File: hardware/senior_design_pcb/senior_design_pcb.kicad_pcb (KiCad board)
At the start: 4 copper layers, 290 x 202.5 mm, 60 parts, among them J1 SBH11-PBPC-D05-ST-BK, J10 1x06Screw-Stepper Driver2, J11 2x08Rectangle-LED Matrix Conn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, J12 1x05JST - Joystick2 connector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, J13 UJ20-C-H-C-4-SMT-TR, J3 1x02JST-IR Transmitter1, J4 1x03JST- IR Receiver1, J5 1x05JST-Admin LCD Console Con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, J6 1x05JST - Joystick1 connector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, J7 1x02JST-IR Transmitter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

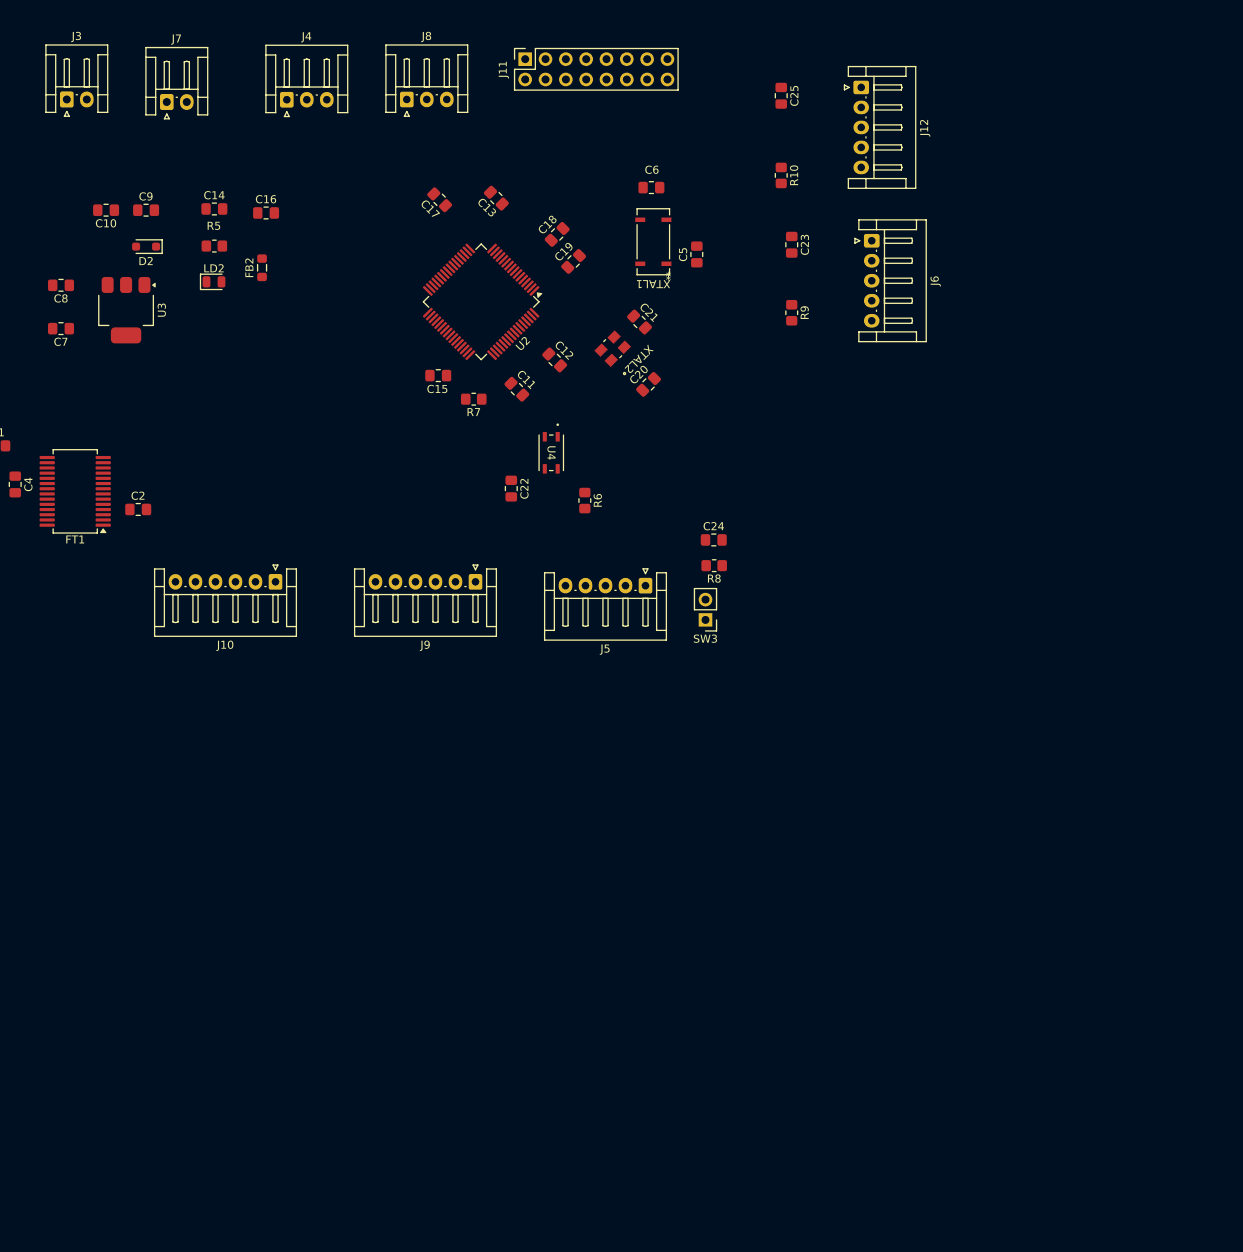
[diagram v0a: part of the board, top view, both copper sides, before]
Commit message: edited schematic pinouts
added test points
edited pinouts for easier traces
added header
added comments
+notes from class today & what to change
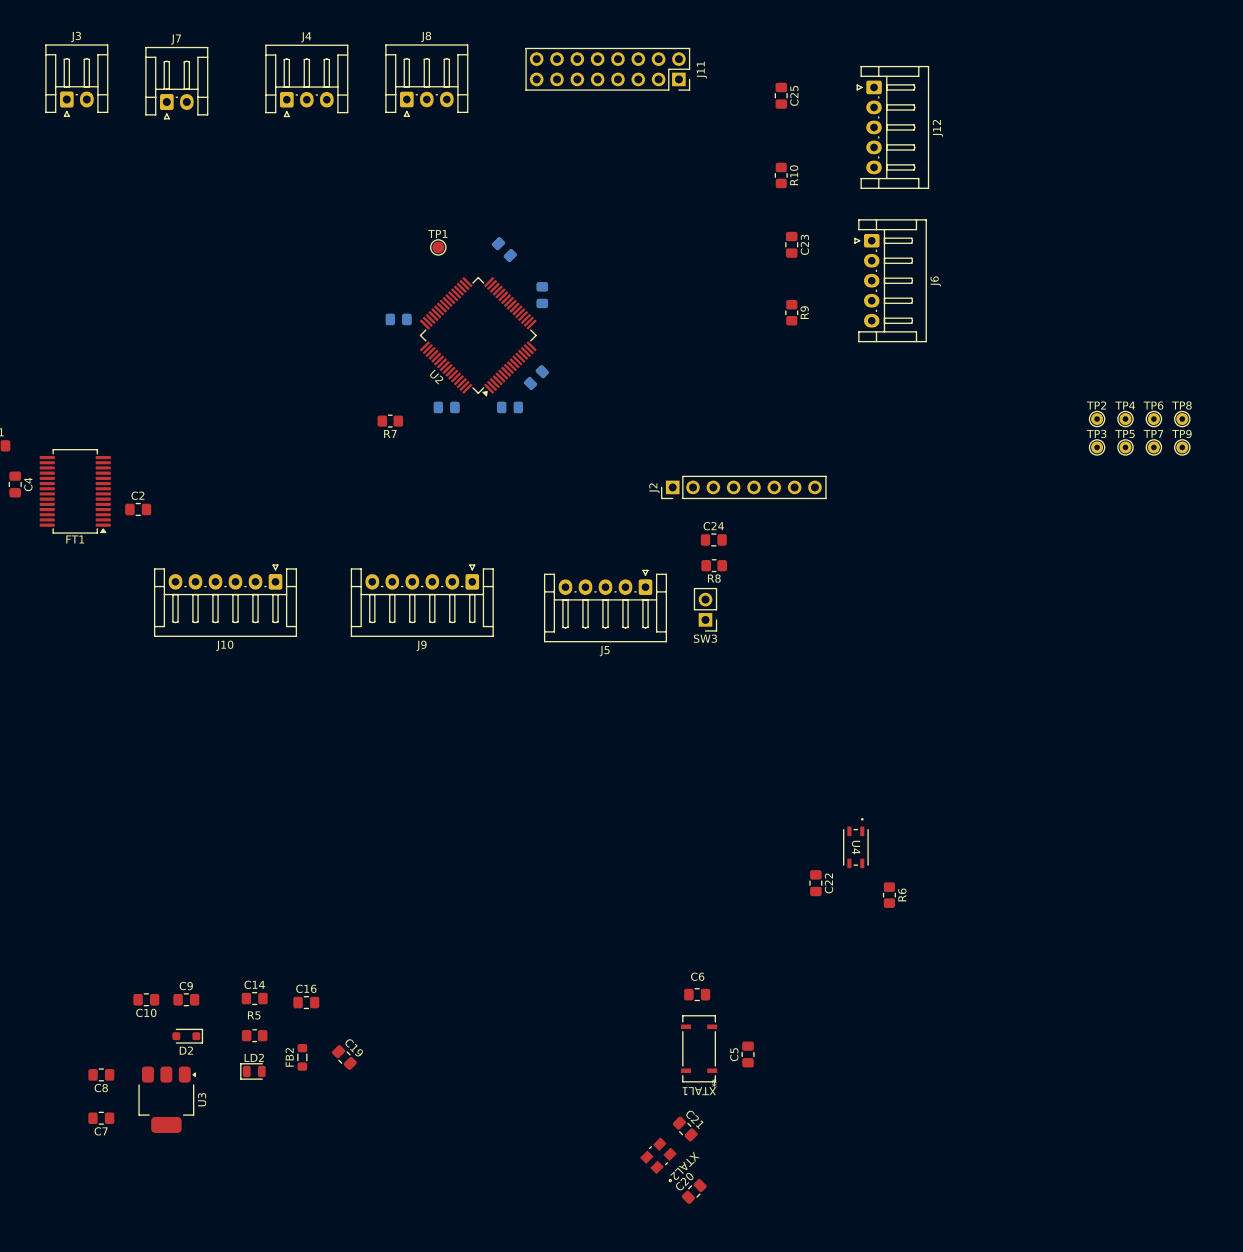
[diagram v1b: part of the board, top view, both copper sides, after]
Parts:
- added J2: Conn_01x08_Pin, Connector_PinHeader_2.54mm:PinHeader_1x08_P2.54mm_Vertical, F.Cu at (132.3, 88.0)
- added TP1: TestPoint_Small, TestPoint:TestPoint_Pad_D1.5mm, F.Cu at (103.0, 58.0)
- added TP2: TestPoint, TestPoint:TestPoint_THTPad_D1.5mm_Drill0.7mm, F.Cu at (185.3, 79.5)
- added TP3: NRST, TestPoint:TestPoint_THTPad_D1.5mm_Drill0.7mm, F.Cu at (185.3, 83.0)
- added TP4: IR-IN1, TestPoint:TestPoint_THTPad_D1.5mm_Drill0.7mm, F.Cu at (188.9, 79.5)
- added TP5: IR-IN2, TestPoint:TestPoint_THTPad_D1.5mm_Drill0.7mm, F.Cu at (188.9, 83.0)
- added TP6: VBUS, TestPoint:TestPoint_THTPad_D1.5mm_Drill0.7mm, F.Cu at (192.4, 79.5)
- added TP7: +5V, TestPoint:TestPoint_THTPad_D1.5mm_Drill0.7mm, F.Cu at (192.4, 83.0)
- added TP8: 3V3, TestPoint:TestPoint_THTPad_D1.5mm_Drill0.7mm, F.Cu at (196.0, 79.5)
- added TP9: GND, TestPoint:TestPoint_THTPad_D1.5mm_Drill0.7mm, F.Cu at (196.0, 83.0)
- C11, C12, C13, C15, C17, C18: moved to B.Cu
- moved C19 103.6 mm to (91.3, 159.3), turned to -45 degrees
- moved C21 101.0 mm to (133.9, 168.2)
- moved C6 101.0 mm to (135.4, 151.4)
- moved XTAL1 101.0 mm to (135.6, 158.2)
- moved C20 101.0 mm to (135.0, 176.0)
- moved XTAL2 101.0 mm to (130.5, 171.5)
- moved C5 100.2 mm to (141.7, 158.9)
- moved C14 98.8 mm to (80.0, 151.9)
- moved C16 98.8 mm to (86.5, 152.4)
- moved R5 98.8 mm to (80.0, 156.5)
- moved C7 98.8 mm to (60.9, 166.8)
- moved FB2 98.8 mm to (86.0, 159.2)
- moved LD2 98.8 mm to (80.0, 161.0)
- moved C10 98.8 mm to (66.5, 152.0)
- moved C8 98.8 mm to (60.9, 161.4)
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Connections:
- net Net-(J13-CC1) renamed /cc1
- net Net-(J13-CC2) renamed /cc2
- net Net-(J13-SHIELD) renamed /usbc-shield
- J10 pad 1: +24V -> unconnected-(J10-Pin_1-Pad1)
- J10 pad 2: /PC6 -> /PC8
- J10 pad 4: /PC8 -> /PC6
- J10 pad 5: /PC9 -> /PB15
- J11 pad 1: /PB11 -> /PA4
- J11 pad 5: /PB1 -> /PA7
- J12 pad 3: /PA0 -> /PA2
- J12 pad 4: /PA1 -> /PA3
- J9 pad 1: +24V -> unconnected-(J9-Pin_1-Pad1)
- J9 pad 2: /PB12 -> /PA10
- J9 pad 3: /PB13 -> /PA9
- J9 pad 4: /PB14 -> /PA8
- J9 pad 5: /PB15 -> /PC9
- U2 pad 16: /OE -> /PA2
- U2 pad 17: /LAT -> /PA3
- U2 pad 20: /CLK -> /PA4
- U2 pad 21: /D -> /G1
- U2 pad 22: /C -> /B1
- U2 pad 23: /B -> /PA7
- U2 pad 24: /A -> /G2
- U2 pad 26: /G2 -> /A
- U2 pad 27: /PB1 -> /B
- U2 pad 28: /B1 -> /PB2
- U2 pad 29: /G1 -> /C
- U2 pad 30: /PB11 -> /D
- U2 pad 33: /PB12 -> /CLK
- U2 pad 34: /PB13 -> /LAT
- U2 pad 35: /PB14 -> /OE
- U2 pad 41: /IR_IN_2 -> /PA8
- U2 pad 42: /IR_IN_1 -> /PA9
- U2 pad 44: /PA11 -> /IR_IN_2
- U2 pad 45: /PA12 -> /IR_IN_1
- U2 pad 55: /ADMIN_CONSOLE-BUTTON -> /PB3
- U2 pad 56: /PB4 -> /ADMIN_CONSOLE-BUTTON

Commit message: Update senior_design_pcb.kicad_pcb
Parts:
- moved C20 114.5 mm to (104.6, 65.6), turned to -90 degrees
- moved C5 107.9 mm to (118.8, 53.5)
- moved C6 107.9 mm to (112.4, 46.0)
- moved XTAL1 107.9 mm to (112.6, 52.8)
- moved XTAL2 107.7 mm to (110.9, 65.6), turned to 0 degrees
- moved C21 100.5 mm to (110.9, 70.4), turned to 180 degrees
- moved C14 99.7 mm to (72.0, 52.5)
- moved C16 99.7 mm to (78.5, 53.0)
- moved C7 99.7 mm to (52.9, 67.5)
- moved FB2 99.7 mm to (78.0, 59.9)
- moved LD2 99.7 mm to (72.0, 61.6)
- moved R5 99.7 mm to (72.0, 57.1)
- moved C10 99.7 mm to (58.5, 52.6)
- moved C8 99.7 mm to (52.9, 62.0)
- moved C9 99.7 mm to (63.5, 52.6)
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
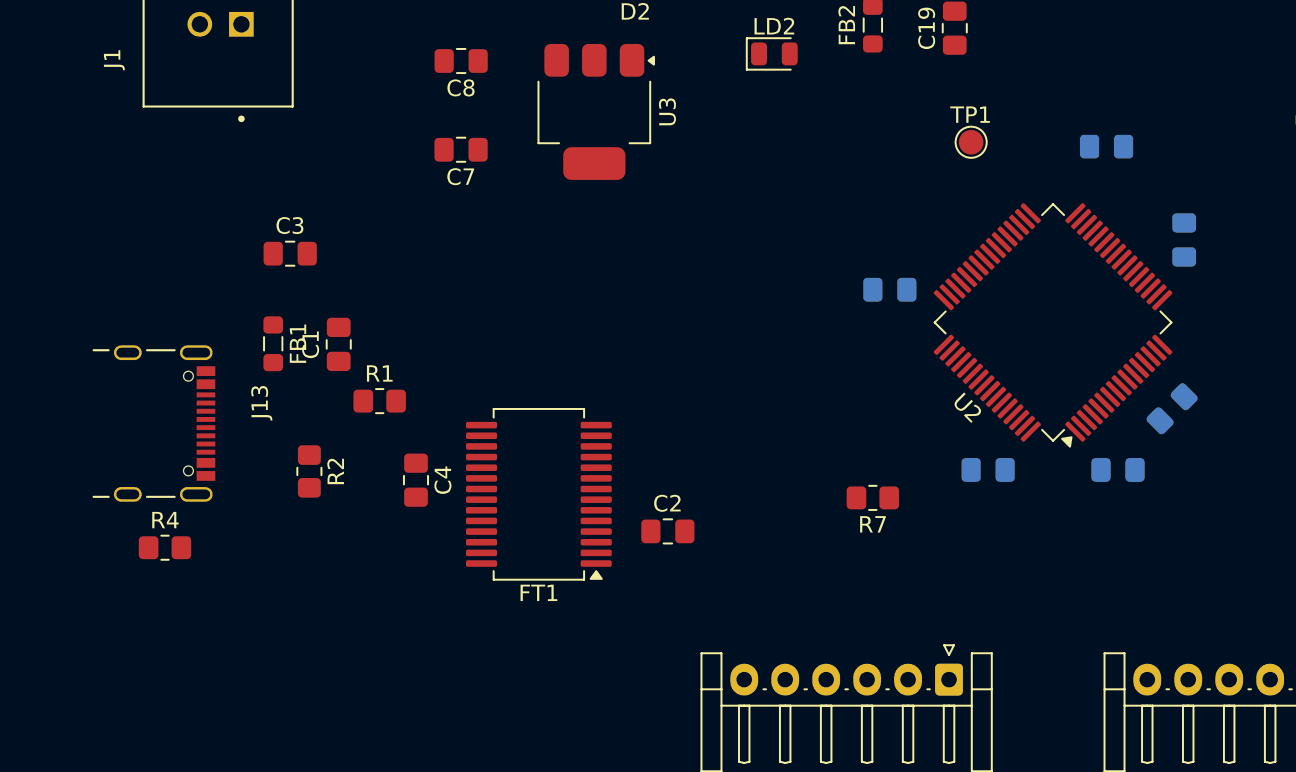
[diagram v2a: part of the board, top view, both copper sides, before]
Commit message: decoupling caps and diffe pair
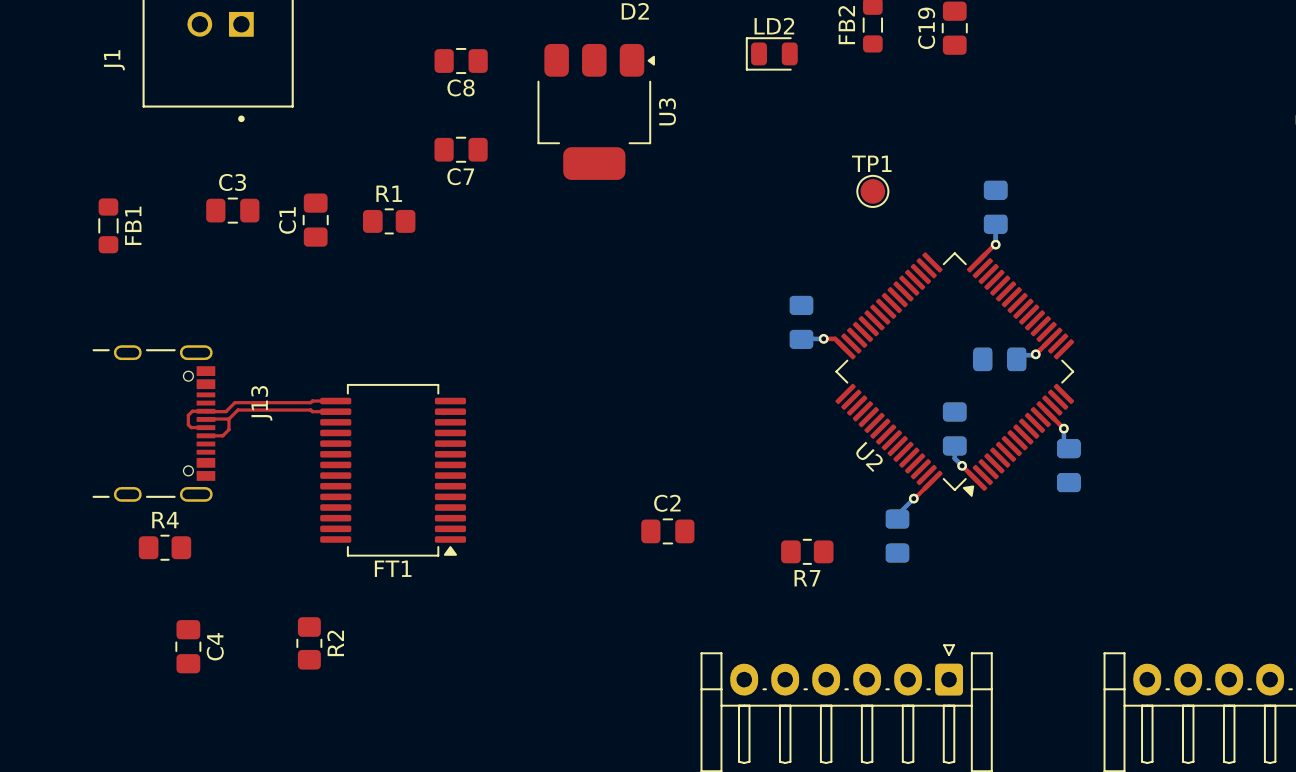
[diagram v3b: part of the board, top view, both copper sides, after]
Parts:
- moved C4 17.2 mm to (36.2, 97.8)
- moved C12 13.4 mm to (85.8, 80.2), turned to 180 degrees
- moved FB1 12.4 mm to (31.3, 72.1)
- moved R1 11.0 mm to (48.5, 71.8)
- moved R2 10.5 mm to (43.6, 97.6)
- moved C11 10.3 mm to (83.0, 84.5), turned to 90 degrees
- moved FT1 9.02 mm to (48.7, 87.0)
- moved C1 7.72 mm to (44.0, 71.8)
- moved C13 7.71 mm to (85.5, 71.0), turned to 90 degrees
- moved C18 7.19 mm to (90.0, 86.7), turned to -90 degrees
- moved C15 6.85 mm to (79.5, 91.0), turned to -90 degrees
- moved TP1 6.71 mm to (78.0, 70.0)
- moved U2 6.71 mm to (83.0, 81.0)
- moved C17 5.75 mm to (73.6, 78.0), turned to 90 degrees
- moved R7 5.18 mm to (74.0, 92.0)
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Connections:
- net +3V0 renamed +3V3
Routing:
- net +3V3: track 0.00 -> 14.1 mm, vias 0 -> 5
- net /D-: track 0.00 -> 11.1 mm
- net /D+: track 0.00 -> 10.4 mm
- net /3VA: track 0.00 -> 2.69 mm, vias 0 -> 1

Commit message: decoupling - usbc + ft232
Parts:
- C1, C2, C3, C4, R1, R2, R4: moved to B.Cu
- moved C4 18.7 mm to (48.7, 83.8), turned to 0 degrees
- moved C3 18.2 mm to (48.7, 86.5)
- moved C2 16.8 mm to (48.7, 89.3), turned to 180 degrees
- moved FB1 13.5 mm to (41.8, 80.7), turned to 180 degrees
- moved R1 13.0 mm to (40.1, 81.8)
- moved R2 12.0 mm to (40.5, 86.0), turned to 0 degrees
- moved C1 7.78 mm to (39.5, 78.1)
- moved R4 7.68 mm to (33.5, 84.2), turned to 180 degrees
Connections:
- net Net-(FT1-3V3OUT) renamed /3v3out
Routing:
- net /VBUS: track 0.00 -> 12.6 mm, vias 0 -> 1
- net /cc1: track 0.00 -> 2.41 mm, vias 0 -> 1
- net /cc2: track 0.00 -> 2.24 mm, vias 0 -> 1

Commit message: updated pcb
shrunk edge cuts
added footprints for pnp
added new symbol for pnp
reorganized stm pinout for easier routing
moved connectors
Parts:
- removed J7: 1x02JST-IR Transmitter, Connector_JST:JST_EH_S2B-EH_1x02_P2.50mm_Horizontal
- removed J8: 1x03JST-IR Receiver2, Connector_JST:JST_EH_S3B-EH_1x03_P2.50mm_Horizontal
- removed TP2: TestPoint, TestPoint:TestPoint_THTPad_D1.5mm_Drill0.7mm
- removed TP3: NRST, TestPoint:TestPoint_THTPad_D1.5mm_Drill0.7mm
- removed TP4: IR-IN1, TestPoint:TestPoint_THTPad_D1.5mm_Drill0.7mm
- removed TP5: IR-IN2, TestPoint:TestPoint_THTPad_D1.5mm_Drill0.7mm
- removed TP6: VBUS, TestPoint:TestPoint_THTPad_D1.5mm_Drill0.7mm
- removed TP7: +5V, TestPoint:TestPoint_THTPad_D1.5mm_Drill0.7mm
- removed TP8: 3V3, TestPoint:TestPoint_THTPad_D1.5mm_Drill0.7mm
- removed TP9: GND, TestPoint:TestPoint_THTPad_D1.5mm_Drill0.7mm
- added C26: .1uF, Capacitor_SMD:C_0805_2012Metric_Pad1.18x1.45mm_HandSolder, F.Cu at (24.9, 91.9)
- added D3: BAT60JFILM, Diode_SMD:D_SOD-323_HandSoldering, F.Cu at (46.0, 73.7)
- added R12: 10K, Resistor_SMD:R_0805_2012Metric_Pad1.20x1.40mm_HandSolder, F.Cu at (56.8, 87.5)
- added R17: 1M, Resistor_SMD:R_0805_2012Metric_Pad1.20x1.40mm_HandSolder, F.Cu at (34.7, 91.7)
- added U1: USBLC6-2SC6Y, kicad_library:TVS-DIODE-USBLC6-2SC6Y, F.Cu at (48.3, 54.6)
- added U5: USBLC6-2SC6Y, kicad_library:TVS-DIODE-USBLC6-2SC6Y, F.Cu at (41.8, 84.7)
- added U6: 2SA1873-GRTE85L_F, kicad_library:TRANS 2PNP-2SA1873, F.Cu at (74.5, 54.3)
- added U7: 2SA1873-GRTE85L_F, kicad_library:TRANS 2PNP-2SA1873, F.Cu at (70.5, 54.4)
- added U8: 2SA1873-GRTE85L_F, kicad_library:TRANS 2PNP-2SA1873, F.Cu at (66.1, 54.3)
- C2, R4: moved to F.Cu
- J10: value 1x06Screw-Stepper Driver2 -> Conn_01x04_Socket; footprint Connector_JST:JST_EH_S6B-EH_1x06_P2.50mm_Horizontal -> Connector_JST:JST_EH_B4B-EH-A_1x04_P2.50mm_Vertical
- J12, J5, J6: footprint Connector_JST:JST_EH_S5B-EH_1x05_P2.50mm_Horizontal -> Connector_JST:JST_EH_B5B-EH-A_1x05_P2.50mm_Vertical
- J3: value 1x02JST-IR Transmitter1 -> Conn_01x02_Socket; footprint Connector_JST:JST_EH_S2B-EH_1x02_P2.50mm_Horizontal -> Connector_JST:JST_EH_B2B-EH-A_1x02_P2.50mm_Vertical
- J4: value 1x03JST- IR Receiver1 -> Conn_01x02_Socket; footprint Connector_JST:JST_EH_S3B-EH_1x03_P2.50mm_Horizontal -> Connector_JST:JST_EH_B2B-EH-A_1x02_P2.50mm_Vertical
- J9: value 1x06Screw-Stepper Driver -> Conn_01x04_Socket; footprint Connector_JST:JST_EH_S6B-EH_1x06_P2.50mm_Horizontal -> Connector_JST:JST_EH_B4B-EH-A_1x04_P2.50mm_Vertical
- XTAL1: value 32.768kHz(12.5pF) -> ECX-.327-CDX-1293; footprint Sr_ Design:ECS - CRYSTAL 32.7680KHZ 6PF SMD -> kicad_library:32KHZ-CLK-ECX1293
- moved C22 136.9 mm to (-30.4, 107.1)
- moved R6 136.9 mm to (-21.2, 108.6)
- moved U4 136.9 mm to (-25.4, 102.6)
- moved TP1 106.9 mm to (-27.0, 50.0)
- moved R7 94.8 mm to (-20.8, 90.9)
- moved J12 91.9 mm to (91.2, 101.8), turned to 90 degrees
- moved SW3 80.5 mm to (55.9, 103.2)
- moved C25 79.6 mm to (86.9, 92.4)
- moved C24 79.5 mm to (58.0, 96.9)
- moved J5 79.4 mm to (49.5, 102.9)
- moved R8 79.2 mm to (58.4, 94.0)
- moved LD2 79.0 mm to (-6.52, 53.1)
- moved R5 78.6 mm to (-6.52, 56.3)
- moved R10 76.9 mm to (83.8, 94.5)
- moved J2 72.9 mm to (61.0, 102.9)
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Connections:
- C2 pad 1: +5V -> Net-(D3-A)
- C20 pad 1: /LS_CLK-IN -> /HS_CLK-IN
- C21 pad 1: /LS_CLK-OUT -> /HS_CLK-OUT
- C5 pad 1: /HS_CLK-IN -> /LS_CLK-IN
- C6 pad 1: /HS_CLK-OUT -> /LS_CLK-OUT
- FB1 pad 1: +5V -> Net-(D3-A)
- FT1 pad 11: unconnected-(FT1-CTS-Pad11) -> Net-(FT1-CTS)
- FT1 pad 15: /D- -> /Dout-
- FT1 pad 16: /D+ -> /Dout+
- J10 pad 1: unconnected-(J10-Pin_1-Pad1) -> /PUL+2
- J10 pad 2: /PC8 -> /DIR+2
- J10 pad 3: /PC7 -> /ENA+2
- J10 pad 4: /PC6 -> GND
- J13 pad A6: /D+ -> /Din +
- J13 pad A7: /D- -> /Din -
- J13 pad B6: /D+ -> /Din +
- J13 pad B7: /D- -> /Din -
- J2 pad 1: /PB5 -> unconnected-(J2-Pin_1-Pad1)
- J2 pad 2: /PB6 -> unconnected-(J2-Pin_2-Pad2)
- J2 pad 3: /PB7 -> unconnected-(J2-Pin_3-Pad3)
- J2 pad 4: /PB8 -> unconnected-(J2-Pin_4-Pad4)
- J2 pad 5: /PB9 -> unconnected-(J2-Pin_5-Pad5)
- J2 pad 6: /PC3 -> unconnected-(J2-Pin_6-Pad6)
- J2 pad 7: /PA0 -> unconnected-(J2-Pin_7-Pad7)
- J2 pad 8: /PA1 -> unconnected-(J2-Pin_8-Pad8)
- J3 pad 1: +5V -> /IR_IN_1-dir
- J4 pad 1: +5V -> /IR_IN_2-dir
- J4 pad 2: /IR_IN_1 -> GND
- J9 pad 1: unconnected-(J9-Pin_1-Pad1) -> /PUL+1
- J9 pad 2: /PA10 -> /DIR+1
- J9 pad 3: /PA9 -> /ENA+1
- J9 pad 4: /PA8 -> GND
- U2 pad 8: /ADMIN_JOYSTICK-X -> /ADMIN_JOYSTICK-Y
- U2 pad 9: /ADMIN_JOYSTICK-Y -> /ADMIN_JOYSTICK-X
- XTAL1 pad 1: /HS_CLK-IN -> /LS_CLK-IN
- XTAL1 pad 2: GND -> /LS_CLK-OUT
- XTAL2 pad 1: /LS_CLK-IN -> /HS_CLK-IN
- XTAL2 pad 3: /LS_CLK-OUT -> /HS_CLK-OUT
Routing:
- net +5V: track 0.00 -> 32.7 mm, vias 0 -> 1
- net +3V3: track 14.1 -> 29.7 mm, vias 5 -> 9
- net /U5V: track 0.00 -> 12.7 mm
- net /D-: track 11.1 -> 0.00 mm
- net /D+: track 10.4 -> 0.00 mm
- net /Din +: track 0.00 -> 5.72 mm
- net /Din -: track 0.00 -> 5.11 mm
- net /Dout+: track 0.00 -> 3.32 mm
- net Net-(LD2-A): track 0.00 -> 3.22 mm
- net /Dout-: track 0.00 -> 3.21 mm
- net /3VA: track 2.69 -> 5.00 mm
- net /3v3out: track 0.00 -> 2.28 mm, vias 0 -> 1
- net Net-(D3-A): track 0.00 -> 2.23 mm
- net /VBUS: track 12.6 -> 10.8 mm
- net /cc2: track 2.24 -> 3.74 mm
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- added copper zone on In2.Cu, net +3V3
- added copper zone on F.Cu, net +5V
- added copper zone on F.Cu, net /3v3-vo
- added copper zone on F.Cu, net /usbc-shield
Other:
- board size 290 x 202.5 mm -> 64.8 x 61.5 mm
